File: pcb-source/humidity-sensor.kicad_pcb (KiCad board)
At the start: 2 copper layers, 3 parts, among them U1 STM32L051C8Tx, U2 SHTC3, U3 SYN115

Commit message: Work on schematic and layout
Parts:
- added AE1: Antenna, TestPoint:TestPoint_THTPad_D2.0mm_Drill1.0mm, F.Cu at (132.8, 119.3)
- added C1: 10pF C0G, Capacitor_SMD:C_0402_1005Metric, F.Cu at (207.2, 105.0)
- added C2: 10pF C0G, Capacitor_SMD:C_0402_1005Metric, F.Cu at (210.2, 105.0)
- added D1: TVS, Diode_SMD:D_SOD-523, F.Cu at (209.8, 81.8)
- added D2: LED, LED_SMD:LED_0603_1608Metric_Castellated, F.Cu at (198.5, 78.8)
- added D3: LED, LED_SMD:LED_0603_1608Metric_Castellated, F.Cu at (188.5, 110.2)
- added FID1: Fiducial, Fiducial:Fiducial_0.5mm_Mask1mm, F.Cu at (130.0, 131.6)
- added FID2: Fiducial, Fiducial:Fiducial_0.5mm_Mask1mm, F.Cu at (158.0, 140.6)
- added FID3: Fiducial, Fiducial:Fiducial_0.5mm_Mask1mm, F.Cu at (157.9, 118.0)
- added H1: MountingHole_Pad, TestPoint:TestPoint_THTPad_D1.5mm_Drill0.7mm, F.Cu at (142.6, 137.4)
- added H2: MountingHole_Pad, TestPoint:TestPoint_THTPad_D1.5mm_Drill0.7mm, F.Cu at (153.1, 137.4)
- added J1: Conn_ARM_JTAG_SWD_10, Connector_PinHeader_1.27mm:PinHeader_2x05_P1.27mm_Vertical_SMD, F.Cu at (180.0, 83.0)
- added Q1: Q_NMOS_GSD, Package_TO_SOT_SMD:SOT-23, F.Cu at (187.7, 78.3)
- added Q2: Q_NMOS_GSD, Package_TO_SOT_SMD:SOT-23, F.Cu at (208.2, 91.5)
- added R1: 300R, Resistor_SMD:R_0402_1005Metric, F.Cu at (197.7, 81.0)
- added R2: 1M, Resistor_SMD:R_0402_1005Metric, F.Cu at (192.2, 110.0)
- added R3: 300R, Resistor_SMD:R_0402_1005Metric, F.Cu at (192.2, 112.0)
- added REF**: OSHW-Symbol_6.7x6mm_Copper, Symbol:OSHW-Symbol_6.7x6mm_Copper, F.Cu at (213.8, 113.8)
- added Y1: 13.56MHz, Crystal:Crystal_SMD_3225-4Pin_3.2x2.5mm, F.Cu at (208.6, 99.2)
- moved U3 60.3 mm to (213.9, 99.8), turned to 180 degrees
- moved U2 49.1 mm to (133.2, 137.2), turned to 180 degrees
- moved U1 47.7 mm to (193.8, 98.8)
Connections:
- U1 pad 1: Net-(U1-Pad1) -> VCC
- U1 pad 23: Net-(U1-Pad23) -> GND
- U1 pad 24: Net-(U1-Pad24) -> VCC
- U1 pad 34: Net-(U1-Pad34) -> /SWDIO
- U1 pad 35: Net-(U1-Pad35) -> GND
- U1 pad 36: Net-(U1-Pad36) -> VCC
- U1 pad 37: Net-(U1-Pad37) -> /SWCLK
- U1 pad 44: Net-(U1-Pad44) -> GND
- U1 pad 47: Net-(U1-Pad47) -> GND
- U1 pad 48: Net-(U1-Pad48) -> VCC
- U1 pad 8: Net-(U1-Pad8) -> GND
- U1 pad 9: Net-(U1-Pad9) -> VCC
- U2 pad 1: Net-(U2-Pad1) -> VCC
- U2 pad 4: Net-(U2-Pad4) -> GND
- U3 pad 2: Net-(U3-Pad2) -> GNDA
- U3 pad 3: Net-(U3-Pad3) -> VCC
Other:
- board outline added: 29.6 x 24.2 mm
- board text added: "AAA"

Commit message: Work on schem and layout
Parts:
- removed the REF** at (213.8, 113.8)
- added C10: 0.1uF, Capacitor_SMD:C_0402_1005Metric, F.Cu at (120.9, 34.9)
- added C11: 0.1uF, Capacitor_SMD:C_0402_1005Metric, F.Cu at (119.7, 36.9)
- added C12: 0.1uF, Capacitor_SMD:C_0402_1005Metric, F.Cu at (123.8, 32.9)
- added C13: 1uF, Capacitor_SMD:C_0402_1005Metric, F.Cu at (119.7, 38.9)
- added C14: 0.1uF, Capacitor_SMD:C_0402_1005Metric, F.Cu at (123.8, 34.9)
- added C4: 0.1uF, Capacitor_SMD:C_0402_1005Metric, F.Cu at (118.0, 32.9)
- added C5: DNU, Capacitor_SMD:C_0402_1005Metric, F.Cu at (116.8, 37.4)
- added C6: DNU, Capacitor_SMD:C_0402_1005Metric, F.Cu at (120.9, 32.9)
- added C7: 10uF, Capacitor_SMD:C_0603_1608Metric, F.Cu at (113.3, 37.6)
- added C8: 0.1uF, Capacitor_SMD:C_0402_1005Metric, F.Cu at (118.0, 34.9)
- added C9: 1uF, Capacitor_SMD:C_0402_1005Metric, F.Cu at (116.8, 39.3)
- added REF**: NPTH-0.5mm, NPTH:NPTH-0.5mm, F.Cu at (107.5, 77.4)
- added REF**: NPTH-0.5mm, NPTH:NPTH-0.5mm, F.Cu at (107.5, 82.5)
- added REF**: NPTH-0.5mm, NPTH:NPTH-0.5mm, F.Cu at (107.5, 80.8)
- added REF**: NPTH-0.5mm, NPTH:NPTH-0.5mm, F.Cu at (107.5, 79.1)
- added REF**: NPTH-0.5mm, NPTH:NPTH-0.5mm, F.Cu at (107.5, 75.8)
- added REF**: NPTH-0.5mm, NPTH:NPTH-0.5mm, F.Cu at (107.5, 74.1)
- added REF**: NPTH-0.5mm, NPTH:NPTH-0.5mm, F.Cu at (107.5, 72.4)
- added Y2: DNU, Crystal:Crystal_SMD_3225-4Pin_3.2x2.5mm, F.Cu at (113.9, 34.1)
- moved D1 120.6 mm to (89.3, 87.1), turned to 180 degrees
- moved Q1 99.6 mm to (88.8, 89.5), turned to 270 degrees
- moved U1 83.3 mm to (126.2, 50.0)
- moved U2 71.8 mm to (81.7, 87.2)
- moved AE1 71.1 mm to (82.2, 69.3)
- moved FID1 71.1 mm to (79.4, 81.5)
- moved Y1 71.1 mm to (158.0, 49.1)
- moved C1 71.1 mm to (156.7, 55.0)
- moved C2 71.1 mm to (159.6, 55.0)
- moved D2 71.1 mm to (147.9, 28.8)
- moved D3 71.1 mm to (137.9, 60.2)
- moved FID2 71.1 mm to (107.4, 90.6)
- moved FID3 71.1 mm to (107.3, 68.0)
- moved H1 71.1 mm to (92.0, 87.5)
- moved H2 71.1 mm to (102.5, 87.5)
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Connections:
- net Net-(Q2-Pad1) renamed /RF_EN
- net Net-(U3-Pad6) renamed /RF_DATA
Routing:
- net VCC: track 0.00 -> 14.9 mm
- net Net-(H1-Pad1): track 0.00 -> 5.22 mm
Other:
- board size 29.6 x 24.2 mm -> 38.7 x 24.2 mm

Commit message: Work on schem and PCB
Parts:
- added C13: 10uF, Capacitor_SMD:C_0603_1608Metric, F.Cu at (86.8, 73.0)
- added C14: 0.1uF, Capacitor_SMD:C_0402_1005Metric, F.Cu at (89.0, 72.3)
- added C15: 100pF C0G, Capacitor_SMD:C_0402_1005Metric, F.Cu at (88.5, 65.2)
- added C17: DNU, Capacitor_SMD:C_0402_1005Metric, F.Cu at (85.5, 63.2)
- added C19: DNU, Capacitor_SMD:C_0402_1005Metric, F.Cu at (136.5, 43.1)
- added C20: 12pF C0G, Capacitor_SMD:C_0402_1005Metric, F.Cu at (88.5, 70.0)
- added C21: DNU, Capacitor_SMD:C_0402_1005Metric, F.Cu at (87.0, 70.5)
- added C22: DNU, Capacitor_SMD:C_0402_1005Metric, F.Cu at (85.6, 69.0)
- added C23: 4.7pF C0G, Capacitor_SMD:C_0402_1005Metric, F.Cu at (84.2, 70.5)
- added C24: 10uF, Capacitor_SMD:C_0603_1608Metric, F.Cu at (86.9, 74.5)
- added C3: 22uF 10V, Capacitor_Tantalum_SMD:CP_EIA-3216-18_Kemet-A, F.Cu at (101.1, 89.8)
- added J2: Conn_02x03_Odd_Even, Connector_PinHeader_2.54mm:PinHeader_2x03_P2.54mm_Vertical_SMD, B.Cu at (112.5, 77.4)
- added L1: 820nH, Inductor_SMD:L_0805_2012Metric, F.Cu at (91.2, 68.2)
- added L2: 68nH, Inductor_SMD:L_0402_1005Metric, F.Cu at (85.6, 70.0)
- added R10: 0R, Resistor_SMD:R_0402_1005Metric, F.Cu at (133.3, 68.6)
- added R4: 100K, Resistor_SMD:R_0402_1005Metric, F.Cu at (139.4, 44.6)
- added R5: 0R, Resistor_SMD:R_0402_1005Metric, F.Cu at (88.5, 63.3)
- added R6: 100K, Resistor_SMD:R_0402_1005Metric, F.Cu at (142.2, 66.5)
- added R7: 10K, Resistor_SMD:R_0402_1005Metric, F.Cu at (85.4, 83.2)
- added R8: 10K, Resistor_SMD:R_0402_1005Metric, F.Cu at (85.4, 85.1)
- added R9: 0R, Resistor_SMD:R_0402_1005Metric, F.Cu at (130.4, 68.6)
- added TP1: TP_RF_EN, TestPoint:TestPoint_Pad_D1.0mm, B.Cu at (75.2, 73.3)
- added TP2: TP_RF_DATA, TestPoint:TestPoint_Pad_D1.0mm, B.Cu at (75.2, 77.0)
- added TP3: TP_HUM_SDA, TestPoint:TestPoint_Pad_D1.0mm, B.Cu at (86.2, 81.5)
- added TP4: TP_HUM_SCL, TestPoint:TestPoint_Pad_D1.0mm, B.Cu at (86.3, 84.8)
- added TP5: TP_UART_RX, TestPoint:TestPoint_Pad_D1.0mm, B.Cu at (104.8, 77.8)
- added TP6: TP_UART_TX, TestPoint:TestPoint_Pad_D1.0mm, B.Cu at (104.7, 82.3)
- added TP7: TP_DEBUG_1, TestPoint:TestPoint_Pad_D1.0mm, B.Cu at (104.7, 75.7)
- added TP8: TP_DEBUG_2, TestPoint:TestPoint_Pad_D1.0mm, B.Cu at (104.7, 84.5)
- added TP9: TP_DEBUG_3, TestPoint:TestPoint_Pad_D1.0mm, B.Cu at (104.7, 80.2)
- moved U3 74.9 mm to (91.4, 71.0), turned to 0 degrees
- moved Q2 74.7 mm to (91.2, 75.7), turned to 90 degrees
- moved C18 67.7 mm to (81.6, 87.8), turned to 180 degrees
- moved C2 67.6 mm to (94.5, 73.2), turned to 270 degrees
- moved Y1 65.3 mm to (96.9, 72.2), turned to 270 degrees
- moved C1 64.3 mm to (94.5, 71.2), turned to 270 degrees
- moved C16 62.8 mm to (81.6, 88.8), turned to 180 degrees
- moved U1 42.9 mm to (97.3, 81.8), turned to 270 degrees
- moved D2 31.2 mm to (133.2, 56.3)
- moved R1 31.2 mm to (132.4, 58.5)
- moved C12 9.42 mm to (129.0, 40.8)
- moved C10 9.42 mm to (126.1, 42.7)
- moved C4 9.42 mm to (123.2, 40.8)
- moved C6 9.42 mm to (126.1, 40.8)
- moved C7 9.42 mm to (118.5, 45.5)
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- renumbered C13 to C16, C14 to C18
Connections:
- C16 pad 1: Net-(C13-Pad1) -> Net-(C16-Pad1)
- C16 pad 2: Net-(C13-Pad2) -> GND
- C18 pad 1: Net-(C14-Pad1) -> Net-(C16-Pad1)
- C18 pad 2: Net-(C14-Pad2) -> GND
- U1 pad 10: Net-(U1-Pad10) -> Net-(R3-Pad1)
- U1 pad 11: Net-(U1-Pad11) -> Net-(R1-Pad1)
- U1 pad 16: Net-(U1-Pad16) -> /RF_EN
- U1 pad 17: Net-(U1-Pad17) -> /RF_DATA
- U1 pad 21: Net-(U1-Pad21) -> /UART_TX
- U1 pad 22: Net-(U1-Pad22) -> /UART_RX
- U1 pad 26: Net-(U1-Pad26) -> /HUM_SCL
- U1 pad 27: Net-(U1-Pad27) -> /HUM_SDA
- U1 pad 43: Net-(U1-Pad43) -> /DEBUG_1
- U1 pad 45: Net-(U1-Pad45) -> /DEBUG_2
- U1 pad 46: Net-(U1-Pad46) -> /DEBUG_3
- U2 pad 1: VCC -> Net-(C16-Pad1)
- U2 pad 2: Net-(U2-Pad2) -> /HUM_SCL
- U2 pad 3: Net-(U2-Pad3) -> /HUM_SDA
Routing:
- net VCC: track 14.9 -> 0.00 mm
- net /HUM_SDA: track 0.00 -> 9.46 mm, vias 0 -> 1
- net /HUM_SCL: track 0.00 -> 5.57 mm, vias 0 -> 1
- net Net-(H1-Pad1): track 5.22 -> 0.00 mm
- net /UART_RX: track 0.00 -> 0.67 mm
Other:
- net class Default: clearance 0.2 -> 0.1524; trace_width 0.25 -> 0.2; via_dia 0.8 -> 0.6; via_drill 0.4 -> 0.3
- rule pad_to_mask_clearance: 0.051 -> 0
- rule solder_mask_min_width: 0.25 -> 0.2
- rule trace_clearance: 0.2 -> 0.1524
- rule trace_min: 0.2 -> 0.1524
- rule via_min_size: 0.4 -> 0.6

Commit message: Work on layout
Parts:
- moved FID1 18.7 mm to (65.8, 85.8)
- moved R5 13.9 mm to (84.9, 76.7)
- moved C1 12.6 mm to (84.5, 79.0)
- moved C2 12.6 mm to (84.5, 80.9)
- moved Y1 12.6 mm to (87.0, 79.9)
- moved C17 12.6 mm to (83.9, 75.7), turned to 90 degrees
- moved U3 12.4 mm to (81.8, 79.0)
- moved L1 12.4 mm to (81.7, 76.2)
- moved C14 11.9 mm to (79.4, 79.4)
- moved C15 11.8 mm to (85.9, 76.7), turned to 90 degrees
- moved C13 10.8 mm to (80.2, 81.5)
- moved C20 10.6 mm to (79.5, 75.7), turned to 270 degrees
- moved C21 7.97 mm to (80.0, 74.2), turned to 180 degrees
- moved L2 6.67 mm to (79.5, 72.8), turned to 270 degrees
- moved C22 6.30 mm to (80.5, 72.8), turned to 90 degrees
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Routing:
- net /HUM_SDA: track 9.46 -> 0.00 mm, vias 1 -> 0
- net /HUM_SCL: track 5.57 -> 0.00 mm, vias 1 -> 0

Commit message: Work on layout
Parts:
- removed R10, R9: 0R, Resistor_SMD:R_0402_1005Metric
- removed the REF** at (107.5, 77.4)
- removed the REF** at (107.5, 82.5)
- removed the REF** at (107.5, 80.8)
- removed the REF** at (107.5, 79.1)
- removed the REF** at (107.5, 75.8)
- removed the REF** at (107.5, 74.1)
- removed the REF** at (107.5, 72.4)
- added REF**: NPTH-0.5mm, NPTH:NPTH-0.5mm, F.Cu at (103.0, 77.4)
- added REF**: NPTH-0.5mm, NPTH:NPTH-0.5mm, F.Cu at (103.0, 82.5)
- added REF**: NPTH-0.5mm, NPTH:NPTH-0.5mm, F.Cu at (103.0, 80.8)
- added REF**: NPTH-0.5mm, NPTH:NPTH-0.5mm, F.Cu at (103.0, 79.1)
- added REF**: NPTH-0.5mm, NPTH:NPTH-0.5mm, F.Cu at (103.0, 75.8)
- added REF**: NPTH-0.5mm, NPTH:NPTH-0.5mm, F.Cu at (103.0, 74.1)
- added REF**: NPTH-0.5mm, NPTH:NPTH-0.5mm, F.Cu at (103.0, 72.4)
- added TP10: TP_SWDIO, TestPoint:TestPoint_Pad_D1.0mm, B.Cu at (97.6, 82.5)
- added TP11: TP_SWDCLK, TestPoint:TestPoint_Pad_D1.0mm, B.Cu at (100.5, 82.2)
- added TP12: TP_nRST, TestPoint:TestPoint_Pad_D1.0mm, F.Cu at (102.2, 74.9)
- moved C19 66.6 mm to (79.5, 77.6), turned to 90 degrees
- moved R4 59.7 mm to (89.6, 77.5), turned to 90 degrees
- moved C12 52.6 mm to (99.5, 84.2), turned to 270 degrees
- moved C8 51.5 mm to (90.0, 82.1), turned to 90 degrees
- moved R2 51.3 mm to (90.0, 73.4), turned to 90 degrees
- moved C6 43.6 mm to (96.3, 72.6), turned to 180 degrees
- moved D2 43.4 mm to (91.8, 69.0), turned to 270 degrees
- moved R1 42.7 mm to (91.8, 71.7), turned to 90 degrees
- moved R6 42.7 mm to (100.5, 75.7)
- moved C10 42.2 mm to (101.7, 77.1), turned to 270 degrees
- moved C11 41.9 mm to (94.3, 73.5)
- moved C4 41.0 mm to (100.2, 74.7)
- moved R3 39.9 mm to (100.8, 71.7), turned to 90 degrees
- moved C9 37.4 mm to (94.4, 72.5)
- moved C5 36.2 mm to (98.2, 72.6), turned to 180 degrees
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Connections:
- C16 pad 1: Net-(C16-Pad1) -> VCC
- C18 pad 1: Net-(C16-Pad1) -> VCC
- R7 pad 1: Net-(C16-Pad1) -> VCC
- R8 pad 1: Net-(C16-Pad1) -> VCC
- TP1 pad 1: Net-(R9-Pad1) -> /RF_EN
- TP2 pad 1: Net-(R10-Pad1) -> /RF_DATA
- U2 pad 1: Net-(C16-Pad1) -> VCC
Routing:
- net VCC: track 0.00 -> 120.0 mm, vias 0 -> 7
- net GND: track 0.00 -> 56.4 mm, vias 0 -> 46
- net GNDA: track 0.00 -> 21.5 mm, vias 0 -> 61
- net /HUM_SCL: track 0.00 -> 18.0 mm
- net /HUM_SDA: track 0.00 -> 16.8 mm
- net Net-(J1-Pad10): track 0.00 -> 12.1 mm
- net /UART_TX: track 0.00 -> 10.6 mm, vias 0 -> 1
- net /UART_RX: track 0.67 -> 10.7 mm, vias 0 -> 1
- net /RF_DATA: track 0.00 -> 9.09 mm
- net /DEBUG_3: track 0.00 -> 8.89 mm
- net /DEBUG_2: track 0.00 -> 8.88 mm
- net /RF_EN: track 0.00 -> 7.77 mm, vias 0 -> 1
- net Net-(C5-Pad1): track 0.00 -> 7.75 mm
- net Net-(C2-Pad2): track 0.00 -> 6.47 mm
- net Net-(AE1-Pad1): track 0.00 -> 5.96 mm
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- added copper zone on B.Cu, net GND
- added copper zone on F.Cu, net GND
- added copper zone on B.Cu, net GNDA
- added copper zone on F.Cu, net GNDA
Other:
- board size 38.7 x 24.2 mm -> 34.2 x 22.6 mm

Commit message: Finish routing
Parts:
- added C25: 0.1uF, Capacitor_SMD:C_0402_1005Metric, F.Cu at (102.0, 75.5)
- added R10: 100K, Resistor_SMD:R_0402_1005Metric, F.Cu at (91.5, 75.2)
- added R9: 100K, Resistor_SMD:R_0402_1005Metric, F.Cu at (91.5, 74.2)
- added TP13: TP_VCC, TestPoint:TestPoint_Pad_D1.0mm, B.Cu at (97.1, 87.8)
- added TP14: TP_GND, TestPoint:TestPoint_Pad_D1.0mm, B.Cu at (98.2, 86.5)
- TP12: moved to B.Cu
- TP5: value TP_UART_RX -> TP_UART_TX
- TP6: value TP_UART_TX -> TP_UART_RX
- moved TP3 10.6 mm to (81.5, 88.8)
- moved TP4 9.58 mm to (80.1, 88.8)
- moved R3 8.93 mm to (92.0, 69.8)
- moved D3 7.50 mm to (93.2, 69.1)
- moved TP12 3.97 mm to (102.7, 71.0)
- moved TP7 3.01 mm to (98.5, 81.5)
- moved TP6 2.80 mm to (96.8, 81.3), turned to 0 degrees
- moved TP8 2.08 mm to (99.5, 78.2)
- moved R1 2.03 mm to (91.0, 69.8)
- moved D2 1.95 mm to (89.8, 69.1)
- moved TP9 1.67 mm to (99.8, 77.0)
- moved TP2 1.27 mm to (91.9, 78.0)
- moved TP5 1.05 mm to (96.8, 80.0), turned to 0 degrees
- moved TP10 0.85 mm to (96.8, 82.6)
- moved TP11 0.40 mm to (100.4, 81.9)
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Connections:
- J2 pad 1: /UART_TX -> /UART_RX
- J2 pad 3: /UART_RX -> /UART_TX
- TP5 pad 1: /UART_RX -> /UART_TX
- TP6 pad 1: /UART_TX -> /UART_RX
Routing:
- net VCC: track 120.0 -> 150.0 mm, vias 7 -> 14
- net /DEBUG_1: track 3.42 -> 29.5 mm, vias 0 -> 1
- net /SWDIO: track 4.24 -> 12.3 mm, vias 0 -> 2
- net /DEBUG_2: track 8.88 -> 15.8 mm, vias 0 -> 1
- net GND: track 56.4 -> 63.2 mm, vias 46 -> 69
- net Net-(R3-Pad1): track 0.00 -> 6.37 mm
- net Net-(R1-Pad1): track 0.00 -> 6.26 mm
- net /UART_TX: track 10.6 -> 16.6 mm
- net /SWCLK: track 4.42 -> 10.3 mm, vias 0 -> 1
- net Net-(C25-Pad1): track 12.1 -> 17.7 mm, vias 0 -> 1
- net /DEBUG_3: track 8.89 -> 14.2 mm, vias 0 -> 1
- net /UART_RX: track 10.7 -> 14.7 mm
- net /RF_DATA: track 9.09 -> 11.6 mm, vias 0 -> 1
- net Net-(R10-Pad1): track 0.00 -> 2.03 mm
- net Net-(R10-Pad2): track 0.00 -> 1.89 mm
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
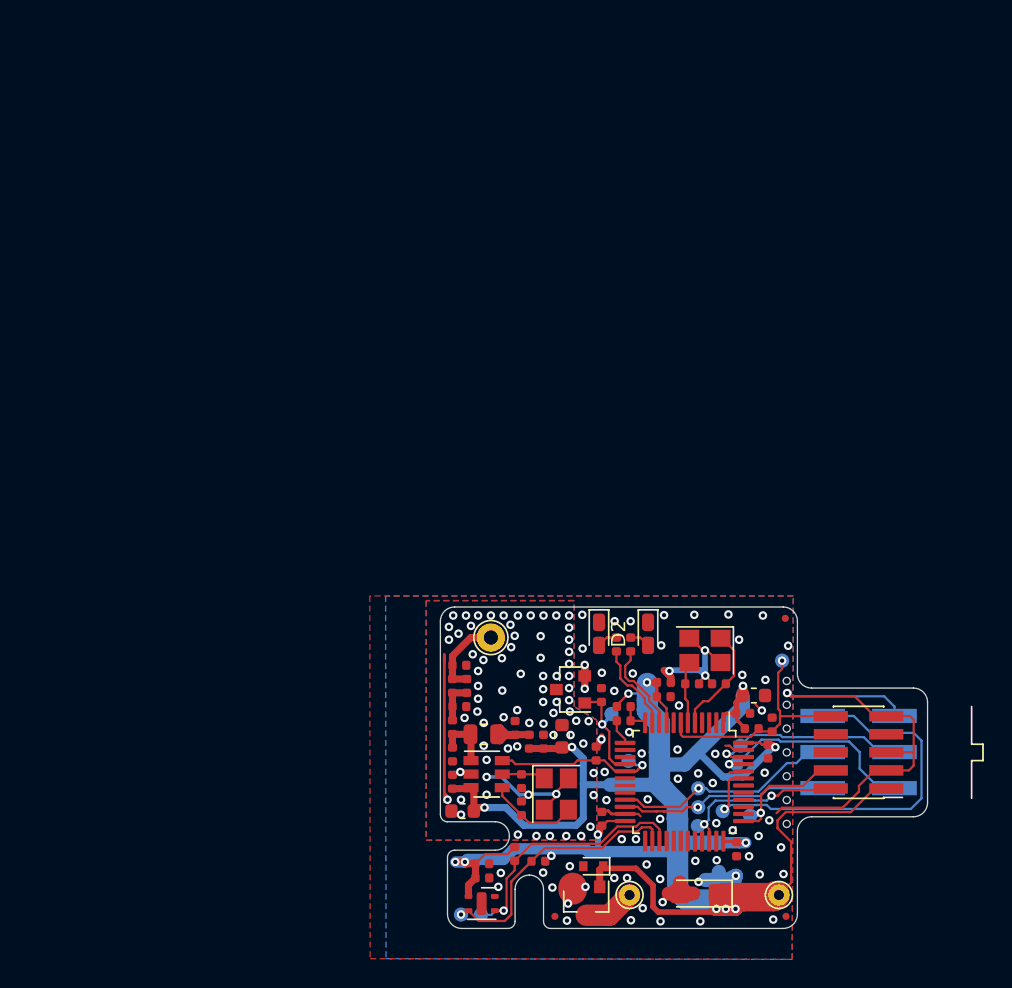
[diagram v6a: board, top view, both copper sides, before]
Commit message: Reduce DRC, add silk
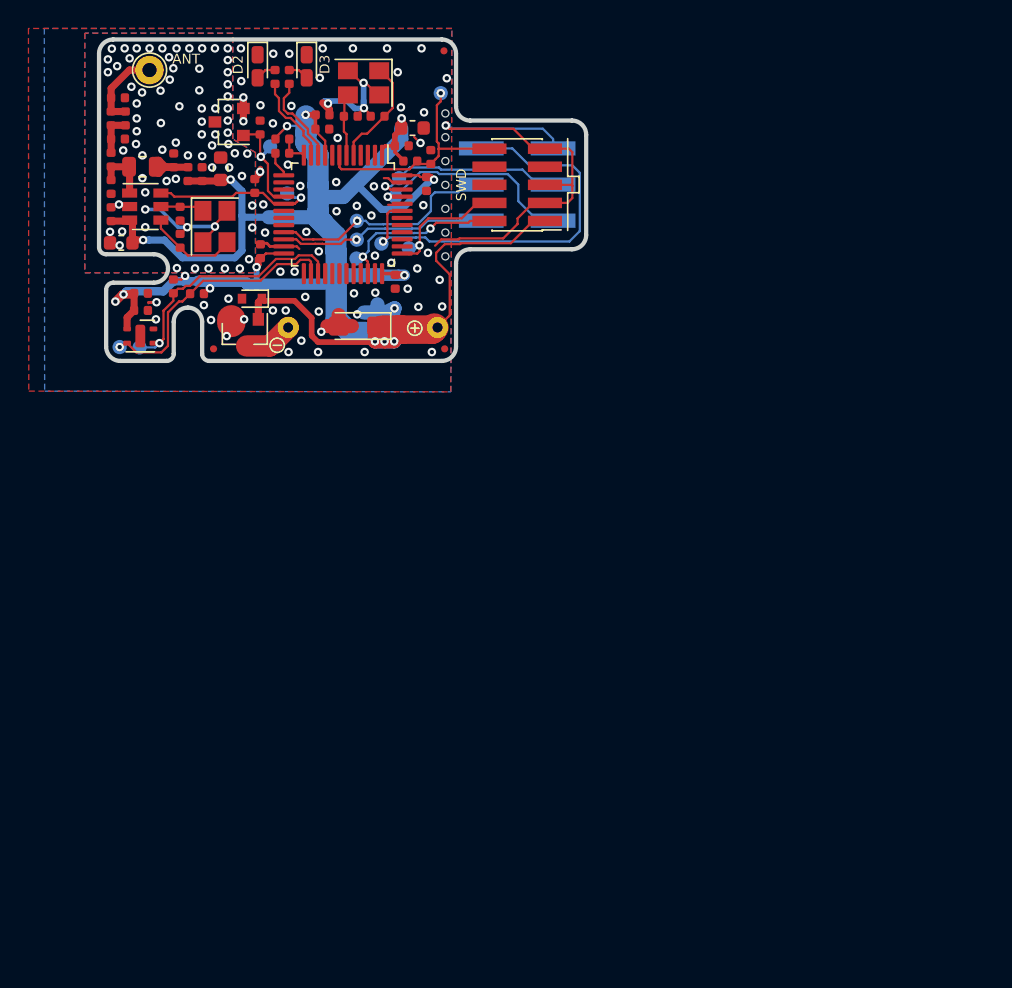
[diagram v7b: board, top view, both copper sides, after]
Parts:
- removed the REF** at (103.0, 77.4)
- removed the REF** at (103.0, 82.5)
- removed the REF** at (103.0, 80.8)
- removed the REF** at (103.0, 79.1)
- removed the REF** at (103.0, 75.8)
- removed the REF** at (103.0, 74.1)
- removed the REF** at (103.0, 72.4)
- added REF**: OSHW-Symbol_6.7x6mm_Copper, Symbol:OSHW-Symbol_6.7x6mm_Copper, B.Cu at (59.6, 34.0)
- added REF**: NPTH-0.5mm, NPTH:NPTH-0.5mm, F.Cu at (79.0, 37.5)
- added REF**: NPTH-0.5mm, NPTH:NPTH-0.5mm, F.Cu at (79.0, 42.5)
- added REF**: NPTH-0.5mm, NPTH:NPTH-0.5mm, F.Cu at (79.0, 40.9)
- added REF**: NPTH-0.5mm, NPTH:NPTH-0.5mm, F.Cu at (79.0, 39.2)
- added REF**: NPTH-0.5mm, NPTH:NPTH-0.5mm, F.Cu at (79.0, 35.9)
- added REF**: NPTH-0.5mm, NPTH:NPTH-0.5mm, F.Cu at (79.0, 34.2)
- added REF**: NPTH-0.5mm, NPTH:NPTH-0.5mm, F.Cu at (79.0, 32.5)
- H1, H2: moved to B.Cu
- moved C16 46.7 mm to (57.6, 45.1)
- moved C13 46.6 mm to (56.2, 41.6)
- moved C15 46.6 mm to (61.9, 36.8)
- moved C17 46.6 mm to (59.9, 35.8)
- moved C20 46.6 mm to (55.5, 35.8)
- moved C21 46.6 mm to (56.0, 34.3)
- moved C25 46.6 mm to (78.0, 35.6)
- moved C8 46.6 mm to (66.0, 42.2)
- moved D2 46.6 mm to (65.8, 29.2)
- moved D3 46.6 mm to (69.2, 29.2)
- moved FID1 46.6 mm to (62.7, 49.0)
- moved FID2 46.6 mm to (79.0, 49.0)
- moved H1 46.6 mm to (68.0, 47.5)
- moved H2 46.6 mm to (78.5, 47.5)
- moved J2 46.6 mm to (84.0, 37.5)
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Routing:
- net GNDA: track 21.5 -> 9.73 mm
- net VCC: track 150.0 -> 147.2 mm, vias 14 -> 15
- net /UART_TX: track 16.6 -> 17.2 mm
- net GND: track 63.2 -> 63.8 mm, vias 69 -> 68
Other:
- board size 34.2 x 22.6 mm -> 34.3 x 22.6 mm
- board text added: "0.1.0"
- board text added: "ANT"
- board text added: "BUG1"
- board text added: "BUG2"
- board text added: "BUG3"
- board text added: "D2"
- board text added: "D3"
- board text added: "GND"
- board text added: "Humidity Sensor"
- board text added: "RF-DATA"
- board text added: "RF-EN"
- board text added: "RST"
- board text added: "RX"
- board text added: "SCL"
- board text added: "SDA"
- board text added: "SWCLK"
- board text added: "SWD"
- board text added: "SWDIO"
- board text added: "TX"
- board text added: "VCC"
